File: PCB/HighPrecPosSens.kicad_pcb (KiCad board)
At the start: 2 copper layers, 60 x 75 mm, 85 parts, among them J1 Conn_01x02_Male, J2 Conn_01x02_Male, J3 Conn_01x02_Male, J4 Conn_01x02_Male, J5 Conn_01x06_Male, U1 ST1S14PHR, U2 S12443, U3 LM393DR2G, U4 LM393DR2G, U5 74LVC541A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

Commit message: Added some text
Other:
- board text added: "Bot"
- board text added: "High Precision Position Sensor (c) 2023 enGyneer by Martin Gyurko"
- board text added: "Top"
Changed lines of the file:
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@@
     )
     (pad_to_mask_clearance 0)
+    (aux_axis_origin 66.85 134.89)
     (pcbplotparams
       (layerselection 0x00010fc_ffffffff)
@@
   )
   (gr_rect (start 66.85 59.89) (end 126.85 134.89) (layer "Edge.Cuts") (width 0.1) (fill none))
+  (gr_text "Top" (at 124 125) (layer "F.Cu")
+    (effects (font (size 1.5 1.5) (thickness 0.3)))
+  )
+  (gr_text "Bot" (at 124 125) (layer "B.Cu")
+    (effects (font (size 1.5 1.5) (thickness 0.3)) (justify mirror))
+  )
+  (gr_text "High Precision\nPosition Sensor\n(c) 2023 enGyneer\nby Martin Gyurko\n" (at 85 64) (layer "F.SilkS")
+    (effects (font (size 1 1) (thickness 0.25)))
+  )
   (dimension (type aligned) (layer "Dwgs.User")
     (pts (xy 66.85 60.5) (xy 66.85 134.89))

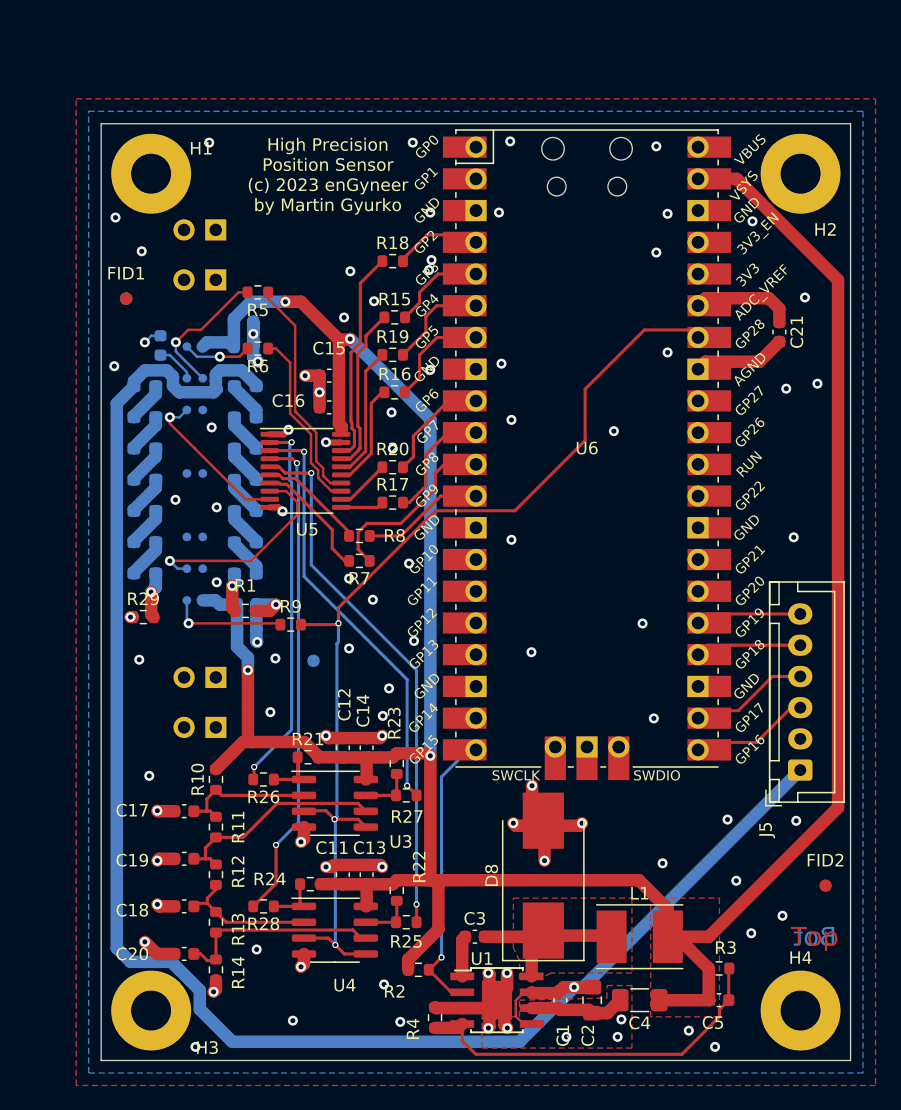
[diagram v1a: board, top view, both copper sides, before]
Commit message: Added some mounting or not definitions
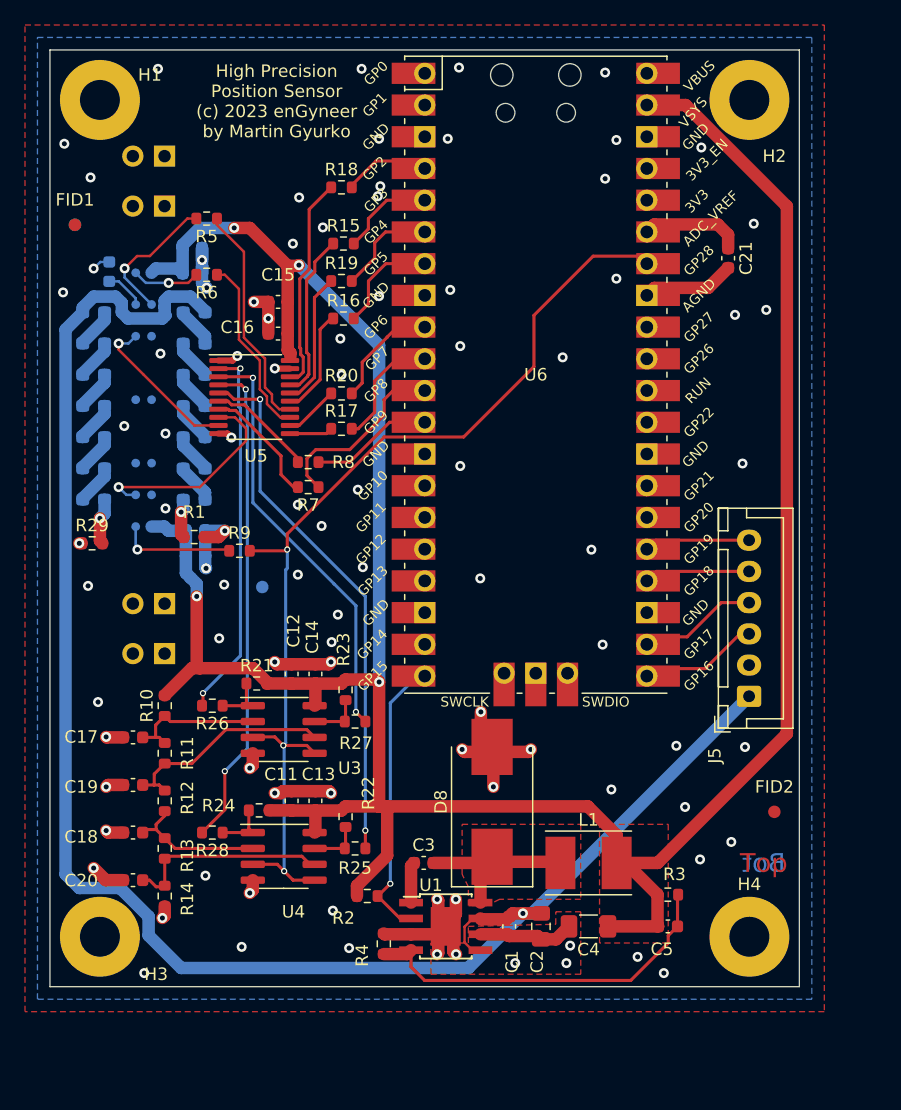
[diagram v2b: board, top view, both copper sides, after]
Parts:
- moved R4 7.19 mm to (89.5, 125.5)
- moved C1 7.19 mm to (99.5, 124.2)
- moved C11 7.19 mm to (82.1, 114.1)
- moved C13 7.19 mm to (84.0, 114.1)
- moved C21 7.19 mm to (117.0, 70.7)
- moved C3 7.19 mm to (92.7, 119.1)
- moved J2 7.19 mm to (71.9, 62.5)
- moved J4 7.19 mm to (71.9, 66.5)
- moved J5 7.19 mm to (118.7, 105.7)
- moved R10 7.19 mm to (71.9, 106.5)
- moved R11 7.19 mm to (71.9, 110.3)
- moved R12 7.19 mm to (71.9, 114.1)
- moved R7 7.19 mm to (83.4, 89.0)
- moved R8 7.19 mm to (83.4, 87.0)
- moved U1 7.19 mm to (94.4, 124.2)
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
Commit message: Added some reasonable testpoints
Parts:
- added J6: Conn_01x02_Male, Connector_PinHeader_2.54mm:PinHeader_1x02_P2.54mm_Vertical, F.Cu at (78.2, 64.8)
- added J7: Conn_01x02_Male, Connector_PinHeader_2.54mm:PinHeader_1x02_P2.54mm_Vertical, F.Cu at (79.0, 91.2)
- added J8: Conn_01x02_Male, Connector_PinHeader_2.54mm:PinHeader_1x02_P2.54mm_Vertical, F.Cu at (78.0, 96.8)
- added TP1: TestPoint, TestPoint:TestPoint_THTPad_D1.5mm_Drill0.7mm, F.Cu at (78.7, 125.0)
- added TP2: TestPoint, TestPoint:TestPoint_THTPad_D1.5mm_Drill0.7mm, F.Cu at (83.8, 125.0)
- added TP3: TestPoint, TestPoint:TestPoint_THTPad_D1.5mm_Drill0.7mm, F.Cu at (81.3, 125.0)
- added TP4: TestPoint, TestPoint:TestPoint_THTPad_D1.5mm_Drill0.7mm, F.Cu at (76.2, 125.0)
- moved FID3 4.15 mm to (83.8, 97.8)
- moved C21 1.72 mm to (116.9, 68.9)
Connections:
- J1 pad 2: unconnected-(J1-Pad2) -> GND
- J2 pad 2: unconnected-(J2-Pad2) -> GND
- J3 pad 2: unconnected-(J3-Pad2) -> GND
- J4 pad 2: unconnected-(J4-Pad2) -> GND
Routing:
- net /D4: track 30.2 -> 57.7 mm
- net /D3: track 34.0 -> 54.5 mm
- net /D2: track 39.4 -> 51.7 mm
- net /D1: track 43.0 -> 53.2 mm
- net +24V: track 136.5 -> 145.6 mm, vias 1 -> 2
- net /EOS: track 16.9 -> 26.0 mm
- net /ST: track 14.7 -> 22.3 mm
- net /Trig: track 12.6 -> 18.0 mm
- net /CLk: track 18.2 -> 21.8 mm
- net /Video: track 9.29 -> 12.3 mm
- net Net-(C21-Pad1): track 8.20 -> 6.74 mm
- net GND: track 78.9 -> 80.1 mm, vias 93 -> 97
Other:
- board text added: "JLCJLCJLCJLC"

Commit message: Added logo
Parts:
- added G1: LOGO, Logos:enGyneer-Logo, F.Cu at (69.6, 82.8)

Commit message: moved logo
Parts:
- moved G1 49.4 mm to (119.0, 80.2), turned to -90 degrees
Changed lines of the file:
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@@
   )
   (footprint "Logos:enGyneer-Logo" (layer "F.Cu")
-    (at 69.6468 82.804 90)
+    (at 119 80.25 -90)
     (property "Mounting" "DNP")
     (property "Sheetfile" "HighPrecPosSens.kicad_sch")
@@
   (via (at 66.250352 119.48051) (size 0.8) (drill 0.4) (layers "F.Cu" "B.Cu") (net 2))
   (via (at 97.25 106.980864) (size 0.8) (drill 0.4) (layers "F.Cu" "B.Cu") (net 2))
-  (via (at 117.6 75.190864) (size 0.8) (drill 0.4) (layers "F.Cu" "B.Cu") (free) (net 2))
+  (via (at 114.25 73.25) (size 0.8) (drill 0.4) (layers "F.Cu" "B.Cu") (free) (net 2))
   (via (at 94.8 73.190864) (size 0.8) (drill 0.4) (layers "F.Cu" "B.Cu") (free) (net 2))
   (via (at 98.25 112.980864) (size 0.8) (drill 0.4) (layers "F.Cu" "B.Cu") (net 2))
@@
   (via (at 114.9 61.790864) (size 0.8) (drill 0.4) (layers "F.Cu" "B.Cu") (free) (net 2))
   (via (at 108.1 72.290864) (size 0.8) (drill 0.4) (layers "F.Cu" "B.Cu") (free) (net 2))
-  (via (at 120.1 74.790864) (size 0.8) (drill 0.4) (layers "F.Cu" "B.Cu") (free) (net 2))
+  (via (at 114 99) (size 0.8) (drill 0.4) (layers "F.Cu" "B.Cu") (free) (net 2))
   (via (at 112.9 109.690864) (size 0.8) (drill 0.4) (layers "F.Cu" "B.Cu") (free) (net 2))
   (via (at 86.7 125.890864) (size 0.8) (drill 0.4) (layers "F.Cu" "B.Cu") (free) (net 2))
@@
   (via (at 80.235 75.480864) (size 0.8) (drill 0.4) (layers "F.Cu" "B.Cu") (net 2))
   (via (at 107.2 55.790864) (size 0.8) (drill 0.4) (layers "F.Cu" "B.Cu") (free) (net 2))
-  (via (at 118.2 87.090864) (size 0.8) (drill 0.4) (layers "F.Cu" "B.Cu") (free) (net 2))
+  (via (at 114.25 86.25) (size 0.8) (drill 0.4) (layers "F.Cu" "B.Cu") (free) (net 2))
   (via (at 104.1 127.090864) (size 0.8) (drill 0.4) (layers "F.Cu" "B.Cu") (free) (net 2))
   (via (at 101.25 109.980864) (size 0.8) (drill 0.4) (layers "F.Cu" "B.Cu") (net 2))

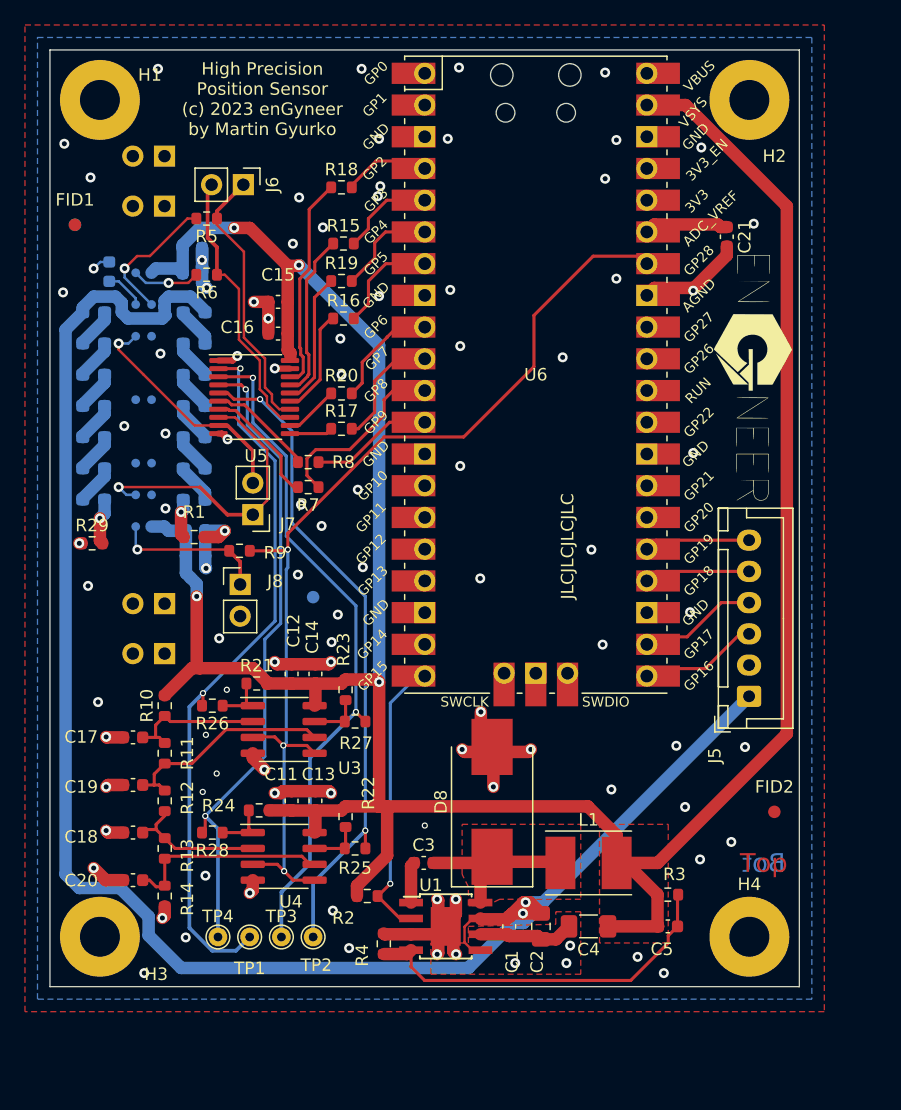
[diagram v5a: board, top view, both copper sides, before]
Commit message: changed vias
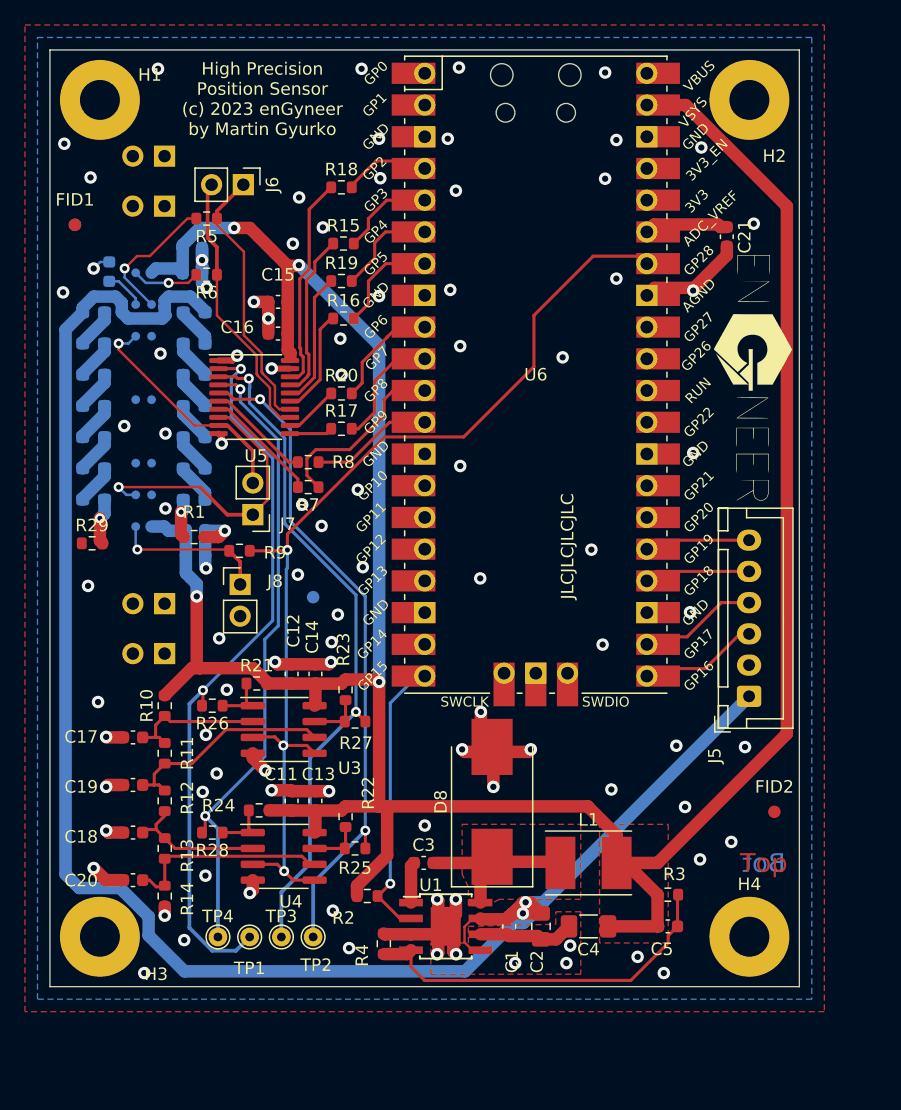
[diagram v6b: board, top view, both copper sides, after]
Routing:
- net /D4: track 57.7 -> 58.3 mm
- net Net-(R7-Pad2): track 9.82 -> 9.32 mm
- net GND: track 80.1 -> 79.9 mm, vias 97 -> 96

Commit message: Some minor changes
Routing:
- net +3.3V: track 231.4 -> 232.4 mm
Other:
- board text added: "Version 1."
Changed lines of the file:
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@@
       (svgprecision 6)
       (excludeedgelayer true)
-      (plotframeref false)
+      (plotframeref true)
       (viasonmask false)
       (mode 1)
@@
       (sketchpadsonfab false)
       (subtractmaskfromsilk false)
-      (outputformat 1)
+      (outputformat 4)
       (mirror false)
-      (drillshape 0)
+      (drillshape 2)
       (scaleselection 1)
       (outputdirectory "Gerber/")
@@
     (effects (font (size 1 1) (thickness 0.2)))
   )
+  (gr_text "Version 1." (at 107.442 108.7628) (layer "F.SilkS")
+    (effects (font (size 1 1) (thickness 0.15)))
+  )
   (gr_text "High Precision\nPosition Sensor\n(c) 2023 enGyneer\nby Martin Gyurko\n" (at 79.756 57.912) (layer "F.SilkS")
     (effects (font (size 1 1) (thickness 0.25)))
@@
   (via (at 119.1 67.890864) (size 1) (drill 0.5) (layers "F.Cu" "B.Cu") (free) (net 2))
   (via (at 80.776001 102.980864) (size 1) (drill 0.5) (layers "F.Cu" "B.Cu") (free) (net 2))
-  (via (at 114.8 118.790864) (size 1) (drill 0.5) (layers "F.Cu" "B.Cu") (free) (net 2))
+  (via (at 114.981543 118.972407) (size 1) (drill 0.5) (layers "F.Cu" "B.Cu") (free) (net 2))
   (via (at 76.75 92.480864) (size 1) (drill 0.5) (layers "F.Cu" "B.Cu") (free) (net 2))
   (via (at 76.9112 105.2068) (size 1) (drill 0.5) (layers "F.Cu" "B.Cu") (free) (net 2))
@@
   (segment (start 76.75 92.480864) (end 75.223 92.480864) (width 1) (layer "B.Cu") (net 2))
   (segment (start 81.785 76.690864) (end 81.785 78.015864) (width 1) (layer "F.Cu") (net 3))
+  (segment (start 121.75 66.496297) (end 121.75 110.5076) (width 1) (layer "F.Cu") (net 3))
   (segment (start 108.12 119.070864) (end 108.855 119.070864) (width 1) (layer "F.Cu") (net 3))
   (segment (start 81.785 71.265864) (end 82.623139 71.265864) (width 1) (layer "F.Cu") (net 3))
   (segment (start 81.785 78.015864) (end 82 78.230864) (width 1) (layer "F.Cu") (net 3))
   (segment (start 111.395 121.610864) (end 111.395 124.100864) (width 1) (layer "F.Cu") (net 3))
-  (segment (start 121.75 108.730864) (end 111.41 119.070864) (width 1) (layer "F.Cu") (net 3))
   (segment (start 79.006792 103.480864) (end 80.131 104.605072) (width 1) (layer "F.Cu") (net 3))
   (segment (start 82.087 104.702864) (end 82.1 104.715864) (width 1) (layer "F.Cu") (net 3))
   (segment (start 81.785 74.150864) (end 81.785 76.690864) (width 1) (layer "F.Cu") (net 3))
   (segment (start 82.087 114.862864) (end 82.1 114.875864) (width 1) (layer "F.Cu") (net 3))
+  (segment (start 113.644567 58.390864) (end 121.75 66.496297) (width 1) (layer "F.Cu") (net 3))
   (segment (start 78.75 68.230864) (end 77.5 68.230864) (width 1) (layer "F.Cu") (net 3))
   (segment (start 89.105 104.585864) (end 89.105 114.505864) (width 1) (layer "F.Cu") (net 3))
@@
   (segment (start 87.33 121.720864) (end 87.33 120.900864) (width 1) (layer "F.Cu") (net 3))
   (segment (start 87.33 120.900864) (end 89.75 118.480864) (width 1) (layer "F.Cu") (net 3))
-  (segment (start 110.54 58.390864) (end 113.644567 58.390864) (width 1) (layer "F.Cu") (net 3))
   (segment (start 88.905 104.385864) (end 89.105 104.585864) (width 1) (layer "F.Cu") (net 3))
   (segment (start 111.395 124.100864) (end 111.445 124.150864) (width 1) (layer "F.Cu") (net 3))
@@
   (segment (start 80.131 104.605072) (end 80.131 104.702864) (width 1) (layer "F.Cu") (net 3))
   (segment (start 81.785 71.265864) (end 78.75 68.230864) (width 1) (layer "F.Cu") (net 3))
-  (segment (start 121.75 66.496297) (end 121.75 108.730864) (width 1) (layer "F.Cu") (net 3))
+  (segment (start 113.186736 119.070864) (end 108.12 119.070864) (width 1) (layer "F.Cu") (net 3))
   (segment (start 81.785 74.150864) (end 81.785 71.265864) (width 1) (layer "F.Cu") (net 3))
   (segment (start 89.75 118.480864) (end 89.75 114.610864) (width 1) (layer "F.Cu") (net 3))
@@
   (segment (start 84.005 106.415864) (end 83.94 106.480864) (width 1) (layer "F.Cu") (net 3))
   (segment (start 80.131 104.702864) (end 82.087 104.702864) (width 1) (layer "F.Cu") (net 3))
-  (segment (start 111.41 119.070864) (end 108.12 119.070864) (width 1) (layer "F.Cu") (net 3))
   (segment (start 80.322 114.862864) (end 82.087 114.862864) (width 1) (layer "F.Cu") (net 3))
   (segment (start 89.685 114.545864) (end 105.815 114.545864) (width 1) (layer "F.Cu") (net 3))
@@
   (segment (start 86.418 104.385864) (end 88.905 104.385864) (width 1) (layer "F.Cu") (net 3))
   (segment (start 86.088 114.875864) (end 86.418 114.545864) (width 1) (layer "F.Cu") (net 3))
-  (segment (start 113.644567 58.390864) (end 121.75 66.496297) (width 1) (layer "F.Cu") (net 3))
   (segment (start 74.5 103.230864) (end 74.75 103.480864) (width 1) (layer "F.Cu") (net 3))
   (segment (start 84.005 114.875864) (end 84.005 116.575864) (width 1) (layer "F.Cu") (net 3))
+  (segment (start 121.75 110.5076) (end 113.186736 119.070864) (width 1) (layer "F.Cu") (net 3))
   (segment (start 82.1 104.715864) (end 84.005 104.715864) (width 1) (layer "F.Cu") (net 3))
+  (segment (start 110.54 58.390864) (end 113.644567 58.390864) (width 1) (layer "F.Cu") (net 3))
   (via (at 82.67873 71.210273) (size 1) (drill 0.5) (layers "F.Cu" "B.Cu") (free) (net 3))
   (via (at 77.5 68.230864) (size 1) (drill 0.5) (layers "F.Cu" "B.Cu") (free) (net 3))
